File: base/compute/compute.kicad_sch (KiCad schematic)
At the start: 19 parts, among them J1 USB_C_Receptacle_USB2.0_16P, J3 Conn_02x20_Counter_Clockwise, U1 MCP1700T-1202ETT, U3 LD1117S33TR_SOT223

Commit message: fixes some mistake in the bom found in first assembly
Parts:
- G1: now left out of the parts list
- H1, H2, H3, H4: now in the parts list
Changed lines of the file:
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@@
 		(unit 1)
 		(exclude_from_sim yes)
-		(in_bom no)
+		(in_bom yes)
 		(on_board yes)
 		(dnp no)
@@
 		(unit 1)
 		(exclude_from_sim yes)
-		(in_bom yes)
+		(in_bom no)
 		(on_board yes)
 		(dnp no)
@@
 		(unit 1)
 		(exclude_from_sim yes)
-		(in_bom no)
+		(in_bom yes)
 		(on_board yes)
 		(dnp no)
@@
 		(unit 1)
 		(exclude_from_sim yes)
-		(in_bom no)
+		(in_bom yes)
 		(on_board yes)
 		(dnp no)
@@
 		(unit 1)
 		(exclude_from_sim yes)
-		(in_bom no)
+		(in_bom yes)
 		(on_board yes)
 		(dnp no)
@@
 		)
 		(instances
-			(project "main_board"
+			(project "compute"
 				(path "/3f5fe6b7-98fc-4d3e-9567-f9f7202d1455"
 					(page "3")
@@
 		)
 		(instances
-			(project "main_board"
+			(project "compute"
 				(path "/3f5fe6b7-98fc-4d3e-9567-f9f7202d1455"
 					(page "2")

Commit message: fixed headers, shifted text base board
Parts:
- J3: farnell# TSM-120-01-L-DV -> 2847240; manf# (none) -> 2213SM-40G-TB
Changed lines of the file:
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@@
 			)
 		)
-		(property "farnell#" "TSM-120-01-L-DV"
+		(property "farnell#" "2847240"
 			(at 222.25 57.15 0)
 			(effects
+				(font
+					(size 1.27 1.27)
+				)
+				(hide yes)
+			)
+		)
+		(property "manf#" "2213SM-40G-TB"
+			(at 222.25 57.15 0)
+			(effects

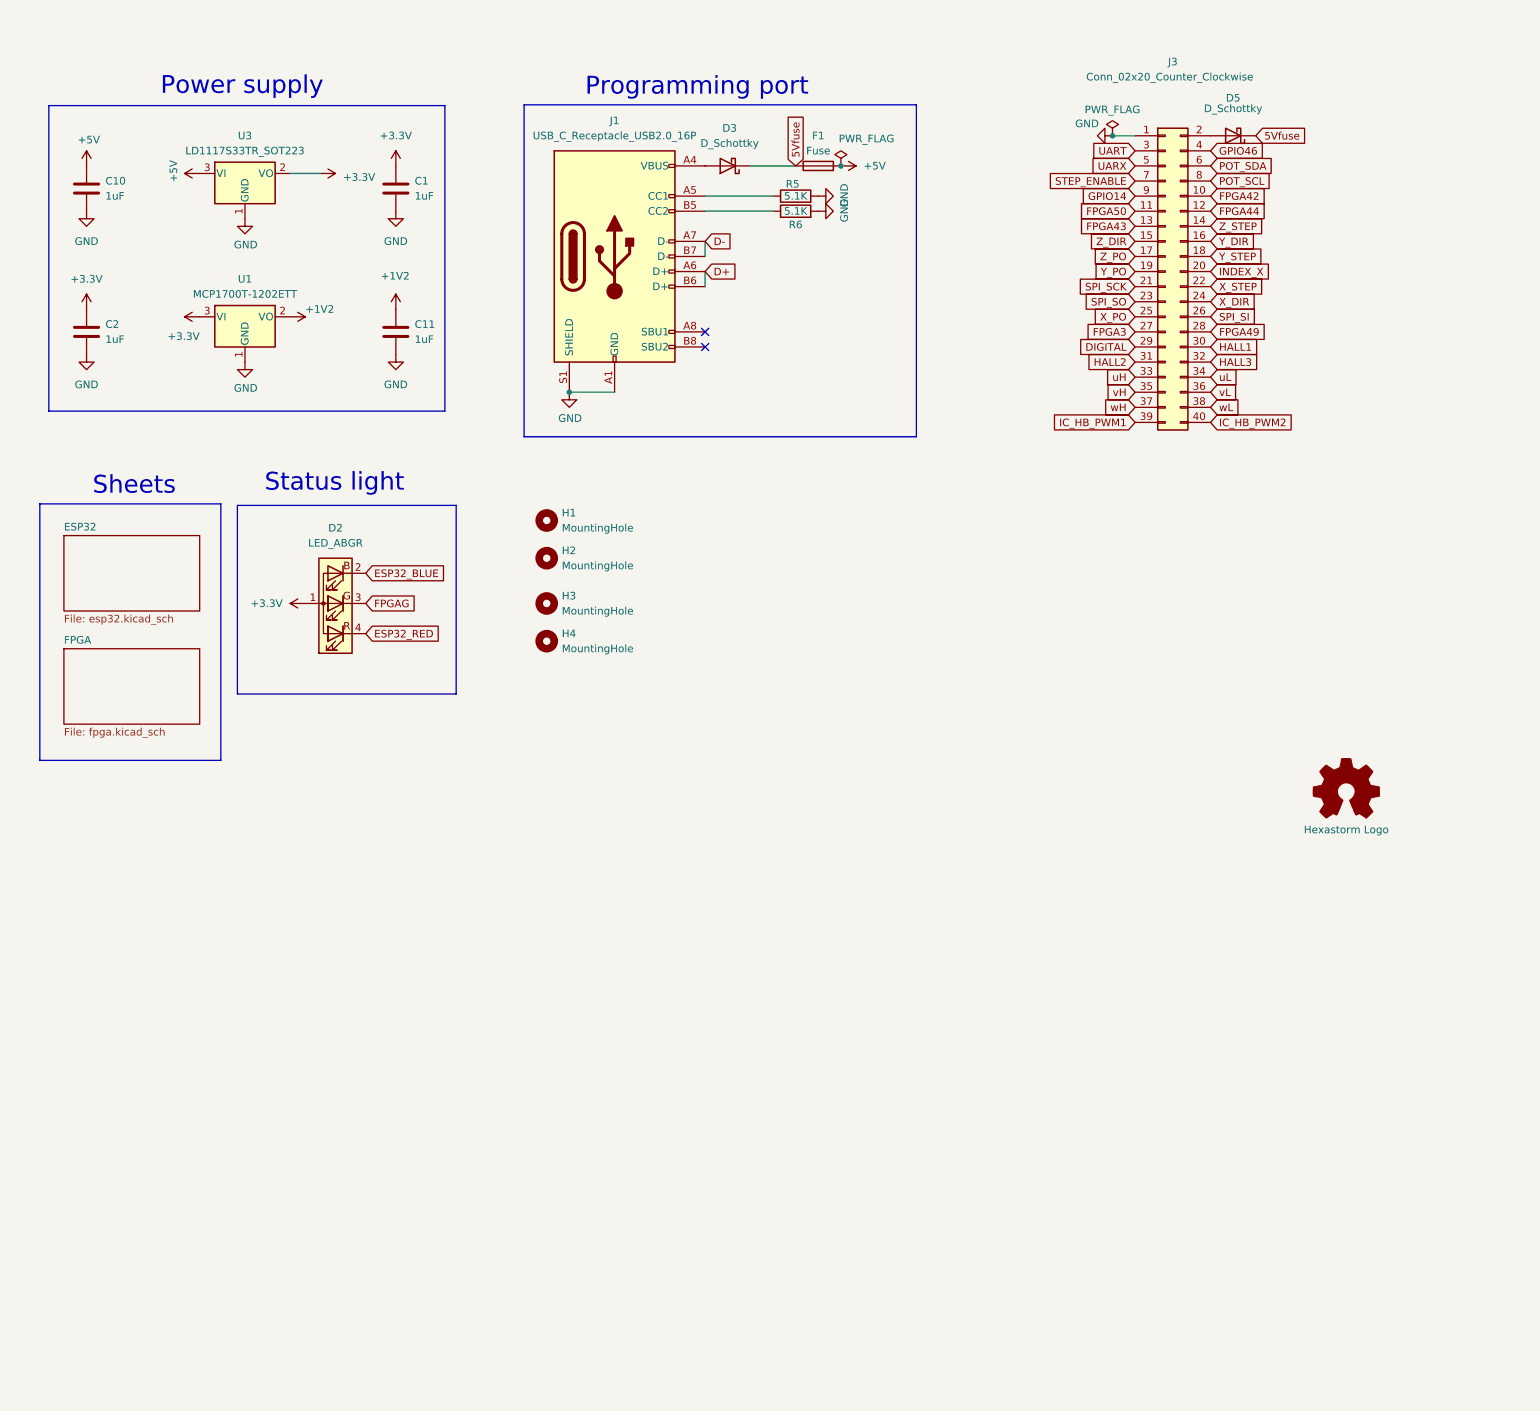
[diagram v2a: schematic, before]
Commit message: compute board 4 layer, with camera connector and small bug fixes
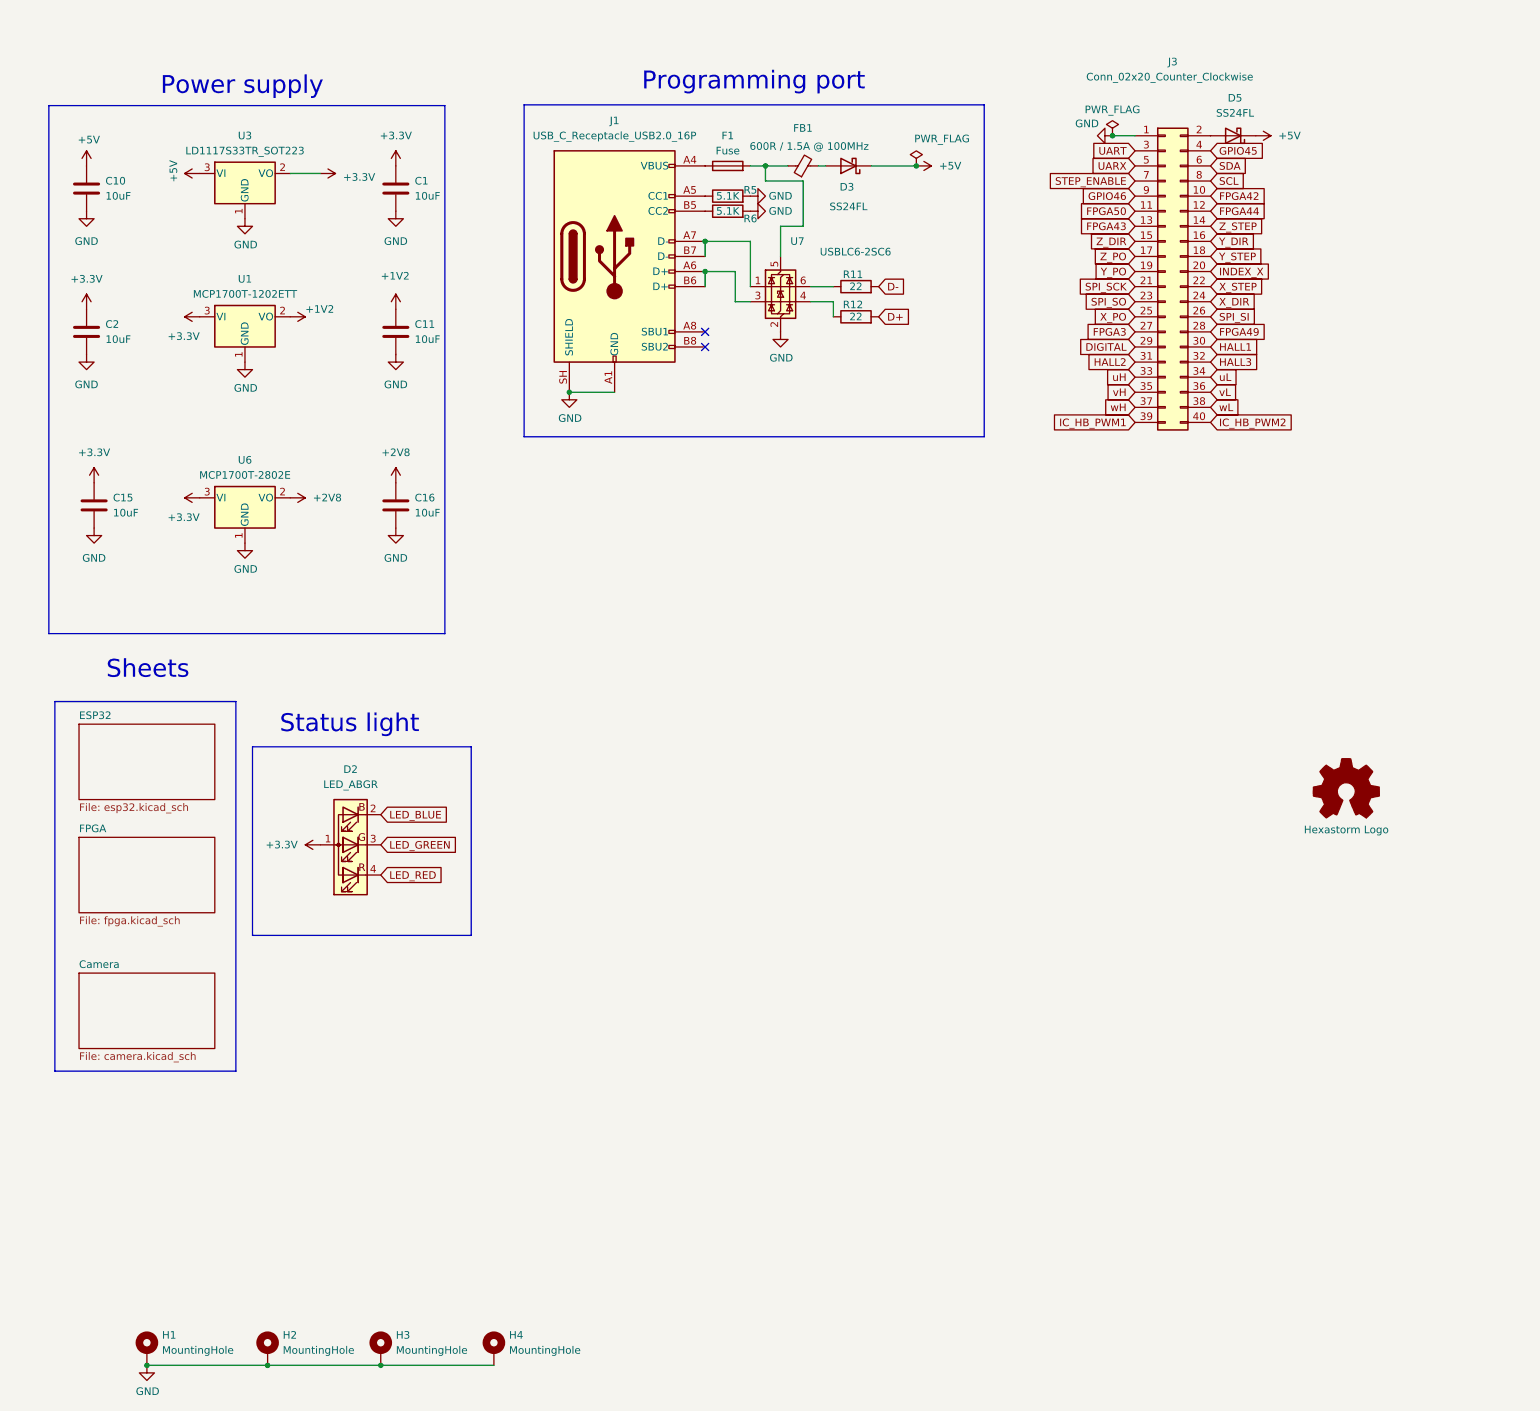
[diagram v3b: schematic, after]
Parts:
- removed D3, D5: D_Schottky, Diode_SMD:D_SOD-323_HandSoldering, symbol Device:D_Schottky
- added C15, C16: 10uF, Capacitor_SMD:C_0805_2012Metric_Pad1.18x1.45mm_HandSolder, symbol Device:C
- added D3, D5: SS24FL, Diode_SMD:D_SMA, symbol Diode:SS24
- added FB1: 600R / 1.5A @ 100MHz, Inductor_SMD:L_0805_2012Metric, symbol Device:FerriteBead_Small
- added R11, R12: 22, Resistor_SMD:R_0805_2012Metric, symbol Device:R
- added U6: MCP1700T-2802E, Package_TO_SOT_SMD:SOT-23, symbol Regulator_Linear:MCP1700x-120xxTT
- added U7: USBLC6-2SC6, Package_TO_SOT_SMD:SOT-23-6, symbol Power_Protection:USBLC6-2SC6
- C1, C10, C11, C2: value 1uF -> 10uF; farnell# 2094043 -> 3013485; manf# 08055C105KAT2A -> CL21B106KOQNNNE; mouser# 581-08055C105KAT2A -> 187-CL21B106KOQNNNE
- F1: footprint Fuse:Fuse_0402_1005Metric_Pad0.77x0.64mm_HandSolder -> Fuse:Fuse_1206_3216Metric; farnell# 2799448 -> 2383294; manf# SF-0402FP100-2 -> 1206L110THYR; mouser# 652-SF-0402FP100-2 -> 576-1206L110THYR
- H1, H2, H3, H4: footprint MountingHole:MountingHole_2.2mm_M2 -> MountingHole:MountingHole_2.2mm_M2_Pad_Via; symbol Mechanical:MountingHole -> Mechanical:MountingHole_Pad; now left out of the parts list
- U3: footprint Package_TO_SOT_SMD:SOT-223-3_TabPin2 -> Package_TO_SOT_SMD:SOT-23
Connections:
- net 5Vfuse is gone; now on an unnamed net: F1.1
- net GPIO14 is gone; now on net GPIO46: J3.9 (Pin_9)
- net +3.3V: now also C15.1, U6.3 (VI)
- net +5V: now also D3.1 (K), D5.1 (K); no longer F1.2
- net D+: now also R12.2; no longer J1.A6 (D+), J1.B6 (D+)
- net D-: now also R11.2; no longer J1.A7 (D-), J1.B7 (D-)
- net GND: now also H1.1, H2.1, H3.1, H4.1, J1.SH (SHIELD), C15.2, C16.2, U6.1 (GND), U7.2 (GND); no longer J1.S1 (SHIELD)
- net GPIO46: no longer J3.4 (Pin_4)
- net at J3.2 (Pin_2): now also D5.2 (A)
- net ESP32_BLUE renamed LED_BLUE
- net ESP32_RED renamed LED_RED
- net FPGAG renamed LED_GREEN
- net POT_SCL renamed SCL
- net POT_SDA renamed SDA
- new net: J1.A7 (D-), J1.B7 (D-), U7.1 (I/O1)
- new net: J1.A6 (D+), J1.B6 (D+), U7.3 (I/O2)
- new net: R12.1, U7.4 (I/O2)
- new net: F1.2, FB1.1, U7.5 (VBUS)
- new net: R11.1, U7.6 (I/O1)
- new net: D3.2 (A), FB1.2
- new net +2V8: C16.1, U6.2 (VO)
- new net GPIO45: J3.4 (Pin_4)
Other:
- added sheet Camera (camera.kicad_sch)
- moved on the sheet: D2, F1, R5, R6

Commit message: schema  extension finished, pre  merge
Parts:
- C1, C10, C11, C15, C16, C2: farnell# 3013485 -> 3010126; manf# CL21B106KOQNNNE -> CL21A106KAYNNNE; mouser# 187-CL21B106KOQNNNE -> 187-CL21A106KAYNNNE
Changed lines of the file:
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@@
 			)
 		)
-		(property "farnell#" "3013485"
+		(property "farnell#" "3010126"
 			(at 92.71 43.18 0)
 			(hide yes)
@@
 			)
 		)
-		(property "manf#" "CL21B106KOQNNNE"
+		(property "manf#" "CL21A106KAYNNNE"
 			(at 92.71 43.18 0)
 			(hide yes)
@@
 			)
 		)
-		(property "mouser#" "187-CL21B106KOQNNNE"
+		(property "mouser#" "187-CL21A106KAYNNNE"
 			(at 92.71 43.18 0)
 			(hide yes)
@@
 			)
 		)
-		(property "farnell#" "3013485"
+		(property "farnell#" "3010126"
 			(at 92.71 67.31 0)
 			(hide yes)
@@
 			)
 		)
-		(property "manf#" "CL21B106KOQNNNE"
+		(property "manf#" "CL21A106KAYNNNE"
 			(at 92.71 67.31 0)
 			(hide yes)
@@
 			)
 		)
-		(property "mouser#" "187-CL21B106KOQNNNE"
+		(property "mouser#" "187-CL21A106KAYNNNE"
 			(at 92.71 67.31 0)
 			(hide yes)
@@
 			)
 		)
-		(property "farnell#" "3013485"
+		(property "farnell#" "3010126"
 			(at 40.64 67.31 0)
 			(hide yes)
@@
 			)
 		)
-		(property "manf#" "CL21B106KOQNNNE"
+		(property "manf#" "CL21A106KAYNNNE"
 			(at 40.64 67.31 0)
 			(hide yes)
@@
 			)
 		)
-		(property "mouser#" "187-CL21B106KOQNNNE"
+		(property "mouser#" "187-CL21A106KAYNNNE"
 			(at 40.64 67.31 0)
 			(hide yes)
@@
 			)
 		)
-		(property "farnell#" "3013485"
+		(property "farnell#" "3010126"
 			(at 92.71 96.52 0)
 			(hide yes)
@@
 			)
 		)
-		(property "manf#" "CL21B106KOQNNNE"
+		(property "manf#" "CL21A106KAYNNNE"
 			(at 92.71 96.52 0)
 			(hide yes)
@@
 			)
 		)
-		(property "mouser#" "187-CL21B106KOQNNNE"
+		(property "mouser#" "187-CL21A106KAYNNNE"
 			(at 92.71 96.52 0)
 			(hide yes)
@@
 			)
 		)
-		(property "farnell#" "3013485"
+		(property "farnell#" "3010126"
 			(at 41.91 96.52 0)
 			(hide yes)
@@
 			)
 		)
-		(property "manf#" "CL21B106KOQNNNE"
+		(property "manf#" "CL21A106KAYNNNE"
 			(at 41.91 96.52 0)
 			(hide yes)
@@
 			)
 		)
-		(property "mouser#" "187-CL21B106KOQNNNE"
+		(property "mouser#" "187-CL21A106KAYNNNE"
 			(at 41.91 96.52 0)
 			(hide yes)
@@
 			)
 		)
-		(property "farnell#" "3013485"
+		(property "farnell#" "3010126"
 			(at 40.64 43.18 0)
 			(hide yes)
@@
 			)
 		)
-		(property "manf#" "CL21B106KOQNNNE"
+		(property "manf#" "CL21A106KAYNNNE"
 			(at 40.64 43.18 0)
 			(hide yes)
@@
 			)
 		)
-		(property "mouser#" "187-CL21B106KOQNNNE"
+		(property "mouser#" "187-CL21A106KAYNNNE"
 			(at 40.64 43.18 0)
 			(hide yes)
